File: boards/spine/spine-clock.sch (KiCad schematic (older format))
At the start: 24 parts, among them U7 iCE40-HX1K-TQ144

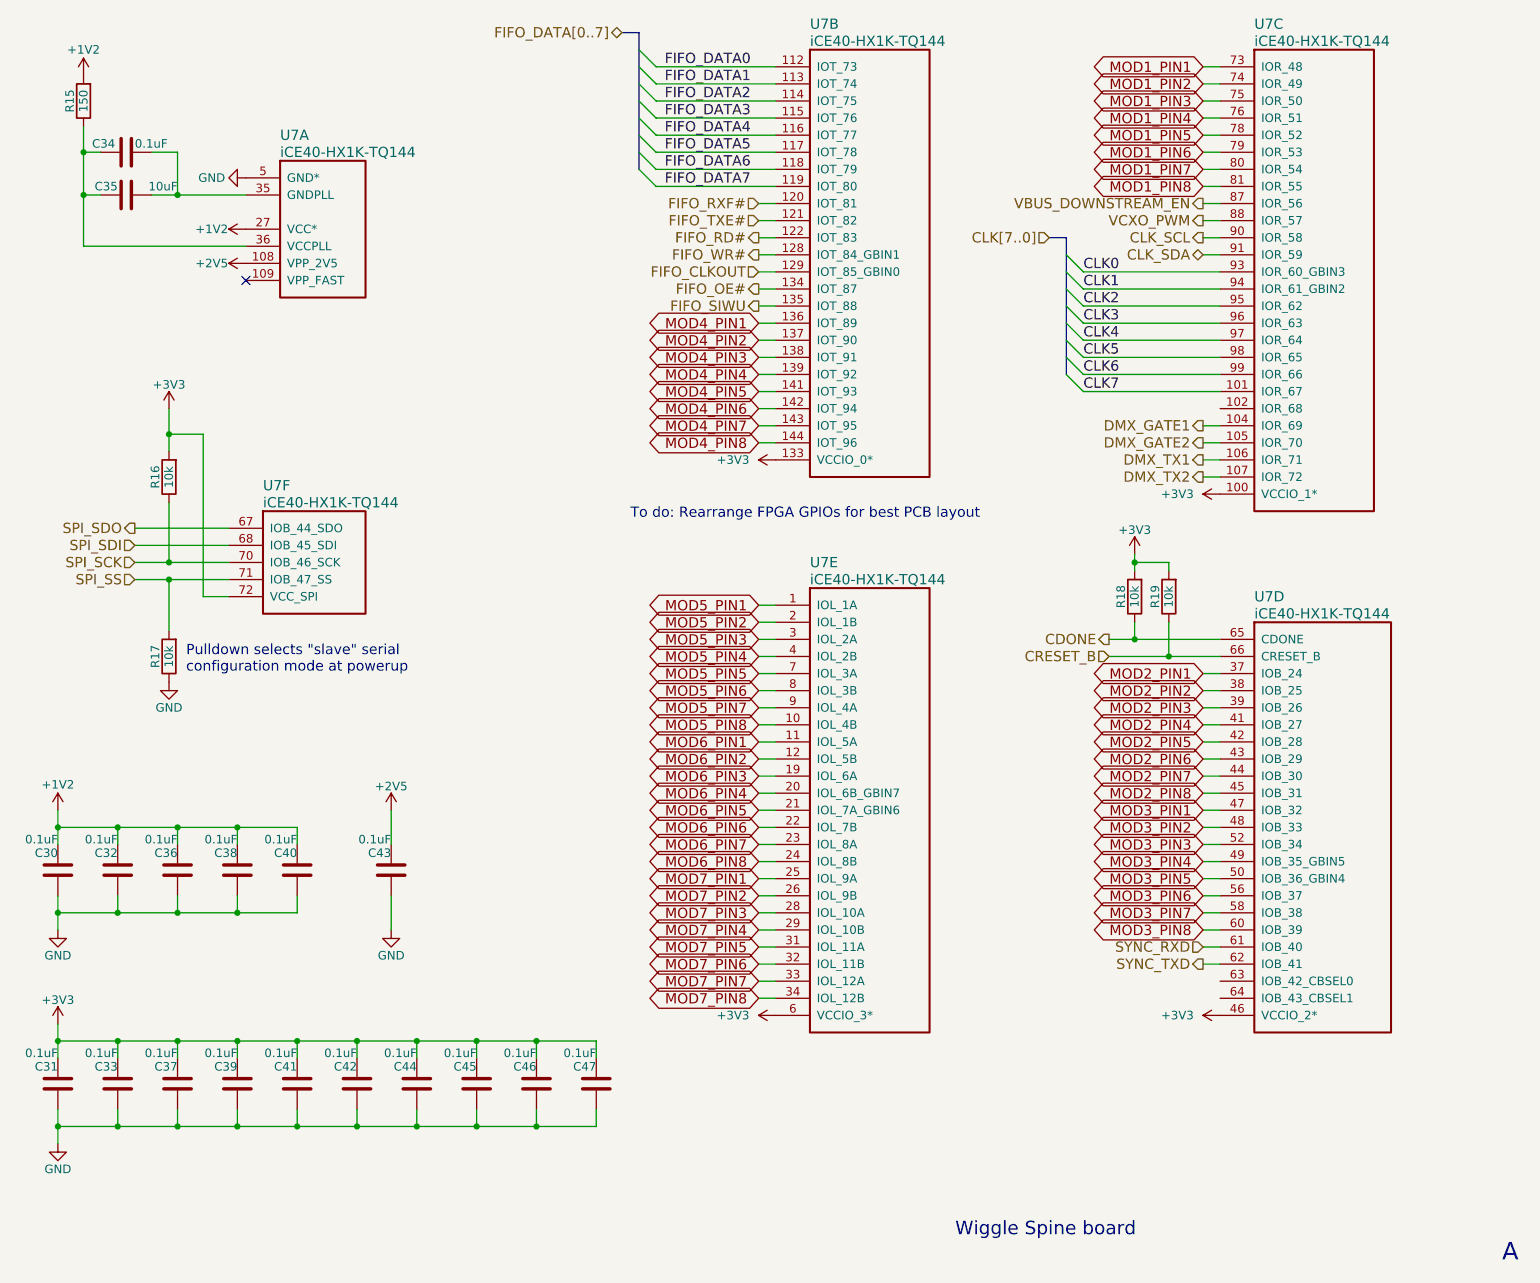
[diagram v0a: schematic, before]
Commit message: Clock generator, sync connectors, title blocks
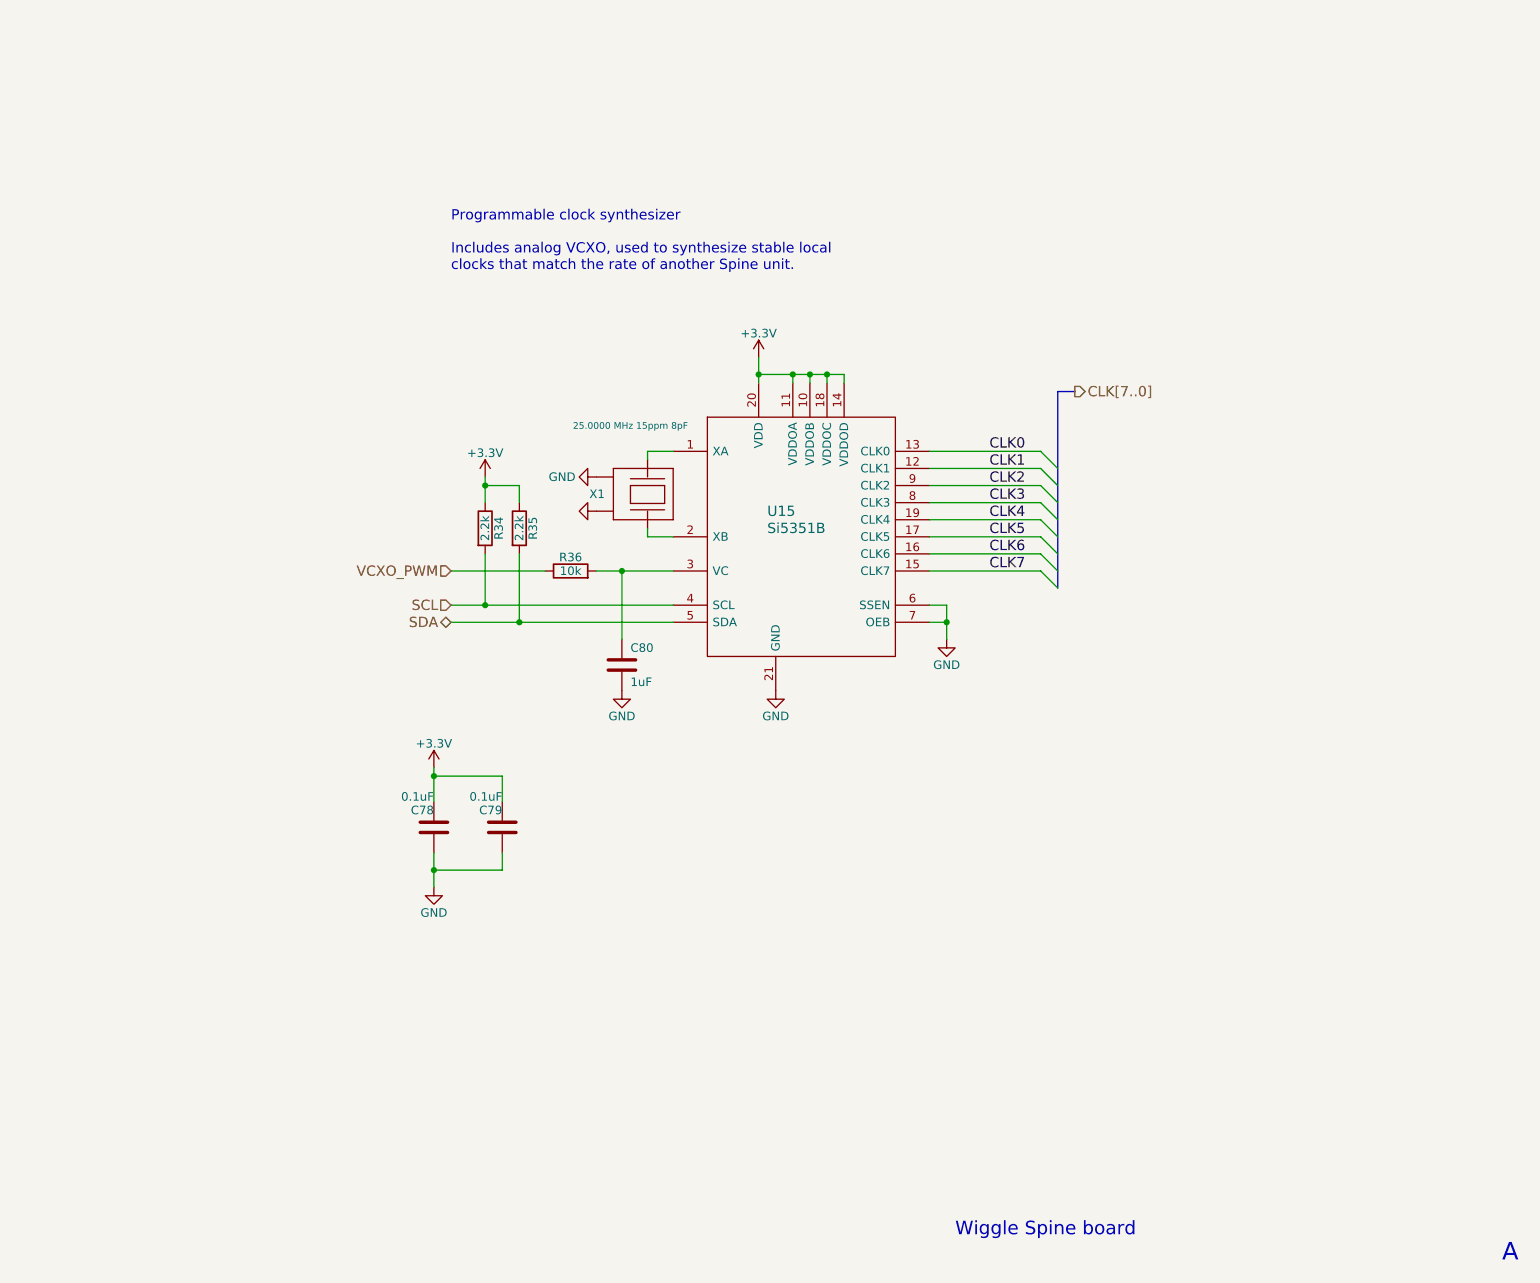
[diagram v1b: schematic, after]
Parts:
- removed C30, C31, C32, C33, C34, C36, C37, C38, C39, C40, C41, C42, C43, C44, C45, C46, C47: 0.1uF, Capacitors_SMD:C_0805, symbol C
- removed C35: 10uF, Capacitors_SMD:C_1206, symbol C
- removed R15: 150, Resistors_SMD:R_0805, symbol R
- removed R16, R17, R18, R19: 10k, Resistors_SMD:R_0805, symbol R
- removed U7: iCE40-HX1K-TQ144, symbol iCE40-HX1K-TQ144
- added C78, C79: 0.1uF, Capacitors_SMD:C_0805, symbol C
- added C80: 1uF, Capacitors_SMD:C_0805, symbol C
- added R34, R35: 2.2k, Resistors_SMD:R_0805, symbol R
- added R36: 10k, Resistors_SMD:R_0805, symbol R
- added U15: Si5351B, Housings_DFN_QFN:QFN-20-1EP_4x4mm_Pitch0.5mm, symbol Si5351B
- added X1: 25.0000 MHz 15ppm 8pF, xess-32X25, symbol XTAL_CHIP32X25
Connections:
- net +3V3: now also C78.2, C79.2, R34.1, R35.1, U15.10 (VDDOB), U15.11 (VDDOA), U15.14 (VDDOD), U15.18 (VDDOC), U15.20 (VDD)
- net CLK0: now also U15.13 (CLK0)
- net CLK1: now also U15.12 (CLK1)
- net CLK2: now also U15.9 (CLK2)
- net CLK3: now also U15.8 (CLK3)
- net CLK4: now also U15.19 (CLK4)
- net CLK5: now also U15.17 (CLK5)
- net CLK6: now also U15.16 (CLK6)
- net CLK7: now also U15.15 (CLK7)
- net GND: now also C78.1, C79.1, C80.2, U15.21 (GND), U15.6 (SSEN), U15.7 (OEB), X1.2, X1.4
- net VCXO_PWM: now also R36.1
- new net: U15.1 (XA), X1.1
- new net: U15.2 (XB), X1.3
- new net: C80.1, R36.2, U15.3 (VC)
- new net SCL: R34.2, U15.4 (SCL)
- new net SDA: R35.2, U15.5 (SDA)
- no-connect marks 1 -> 0
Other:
- note added: "Programmable clock synthesizer\n\nIncludes analog VCXO, used to synthesize stable local\nclocks that match the rate of another Spine unit."
- note removed: "Pulldown selects "slave" serial\nconfiguration mode at powerup"
- note removed: "To do: Rearrange FPGA GPIOs for best PCB layout"

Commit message: Schematic footprint and refdes work
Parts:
- X1: footprint xess-32X25 -> Crystals:crystal_FA238-TSX3225
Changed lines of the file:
@@
 $EndComp
 $Comp
-L GND #PWR0150
+L GND #PWR157
 U 1 1 564F7F28
 P 5650 4550
-F 0 "#PWR0150" H 5650 4300 50  0001 C CNN
+F 0 "#PWR157" H 5650 4300 50  0001 C CNN
 F 1 "GND" H 5650 4400 50  0000 C CNN
 F 2 "" H 5650 4550 60  0000 C CNN
@@
 $EndComp
 $Comp
-L +3.3V #PWR0151
+L +3.3V #PWR156
 U 1 1 564F7F3F
 P 5550 2600
-F 0 "#PWR0151" H 5550 2450 50  0001 C CNN
+F 0 "#PWR156" H 5550 2450 50  0001 C CNN
 F 1 "+3.3V" H 5550 2740 50  0000 C CNN
 F 2 "" H 5550 2600 60  0000 C CNN
@@
 F 0 "X1" V 4900 3150 50  0000 R CNN
 F 1 "25.0000 MHz 15ppm 8pF" V 4500 3300 39  0000 C CNN
-F 2 "xess-32X25" H 4900 3550 50  0001 C CNN
+F 2 "Crystals:crystal_FA238-TSX3225" H 4900 3550 50  0001 C CNN
 F 3 "http://www.ndk.com/images/products/catalog/c_NX3225SA-STD-CSR-3_e.pdf" H 4900 3400 60  0001 C CNN
 F 4 "Digikey" H 4900 3400 60  0001 C CNN "Vend1"
@@
 	4900 3650 5050 3650
 $Comp
-L GND #PWR0152
+L GND #PWR153
 U 1 1 564FA8B8
 P 4600 3300
-F 0 "#PWR0152" H 4600 3050 50  0001 C CNN
+F 0 "#PWR153" H 4600 3050 50  0001 C CNN
 F 1 "GND" V 4600 3100 50  0000 C CNN
 F 2 "" H 4600 3300 60  0000 C CNN
@@
 $EndComp
 $Comp
-L GND #PWR0153
+L GND #PWR158
 U 1 1 564FA968
 P 6650 4250
-F 0 "#PWR0153" H 6650 4000 50  0001 C CNN
+F 0 "#PWR158" H 6650 4000 50  0001 C CNN
 F 1 "GND" H 6650 4100 50  0000 C CNN
 F 2 "" H 6650 4250 60  0000 C CNN
@@
 $EndComp
 $Comp
-L +3.3V #PWR0154
+L +3.3V #PWR152
 U 1 1 564FABDD
 P 3950 3300
-F 0 "#PWR0154" H 3950 3150 50  0001 C CNN
+F 0 "#PWR152" H 3950 3150 50  0001 C CNN
 F 1 "+3.3V" H 3950 3440 50  0000 C CNN
 F 2 "" H 3950 3300 60  0000 C CNN
@@
 $EndComp
 $Comp
-L GND #PWR0155
+L GND #PWR154
 U 1 1 564FE031
 P 4600 3500
-F 0 "#PWR0155" H 4600 3250 50  0001 C CNN
+F 0 "#PWR154" H 4600 3250 50  0001 C CNN
 F 1 "GND" H 4600 3350 50  0001 C CNN
 F 2 "" H 4600 3500 60  0000 C CNN
@@
 $EndComp
 $Comp
-L GND #PWR0156
+L GND #PWR155
 U 1 1 564FE16F
 P 4750 4550
-F 0 "#PWR0156" H 4750 4300 50  0001 C CNN
+F 0 "#PWR155" H 4750 4300 50  0001 C CNN
 F 1 "GND" H 4750 4400 50  0000 C CNN
 F 2 "" H 4750 4550 60  0000 C CNN
@@
 	4300 3850 3750 3850
 $Comp
-L +3.3V #PWR0157
+L +3.3V #PWR150
 U 1 1 564FE49E
 P 3650 5000
-F 0 "#PWR0157" H 3650 4850 50  0001 C CNN
+F 0 "#PWR150" H 3650 4850 50  0001 C CNN
 F 1 "+3.3V" H 3650 5140 50  0000 C CNN
 F 2 "" H 3650 5000 60  0000 C CNN
@@
 $EndComp
 $Comp
-L GND #PWR0158
+L GND #PWR151
 U 1 1 564FE4DC
 P 3650 5700
-F 0 "#PWR0158" H 3650 5450 50  0001 C CNN
+F 0 "#PWR151" H 3650 5450 50  0001 C CNN
 F 1 "GND" H 3650 5550 50  0000 C CNN
 F 2 "" H 3650 5700 60  0000 C CNN
@@
 FB 59 00 E6 A5 69 3A 37 9E CF 73 BC F7 37 E3 33 5D 9E A8 3E 7F 80 FA F7 F6 BB 44 F4 6E D4 E7 77
 A2 1E 1F 27 A2 E3 16 70 32 E9 54 FE 3F E7 AF 00 CA 1C A3 36 0A 00 00 00 00 49 45 4E 44 AE 42 60
-82 70
+82 00
 EndData
 $EndBitmap
